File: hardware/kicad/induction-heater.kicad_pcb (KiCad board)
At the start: 2 copper layers, 21 parts, among them J1 Screw_Terminal_01x01, J2 Screw_Terminal_01x01, J3 Screw_Terminal_01x02, Q1 Q_NMOS_DGS, Q2 Q_NMOS_DGS

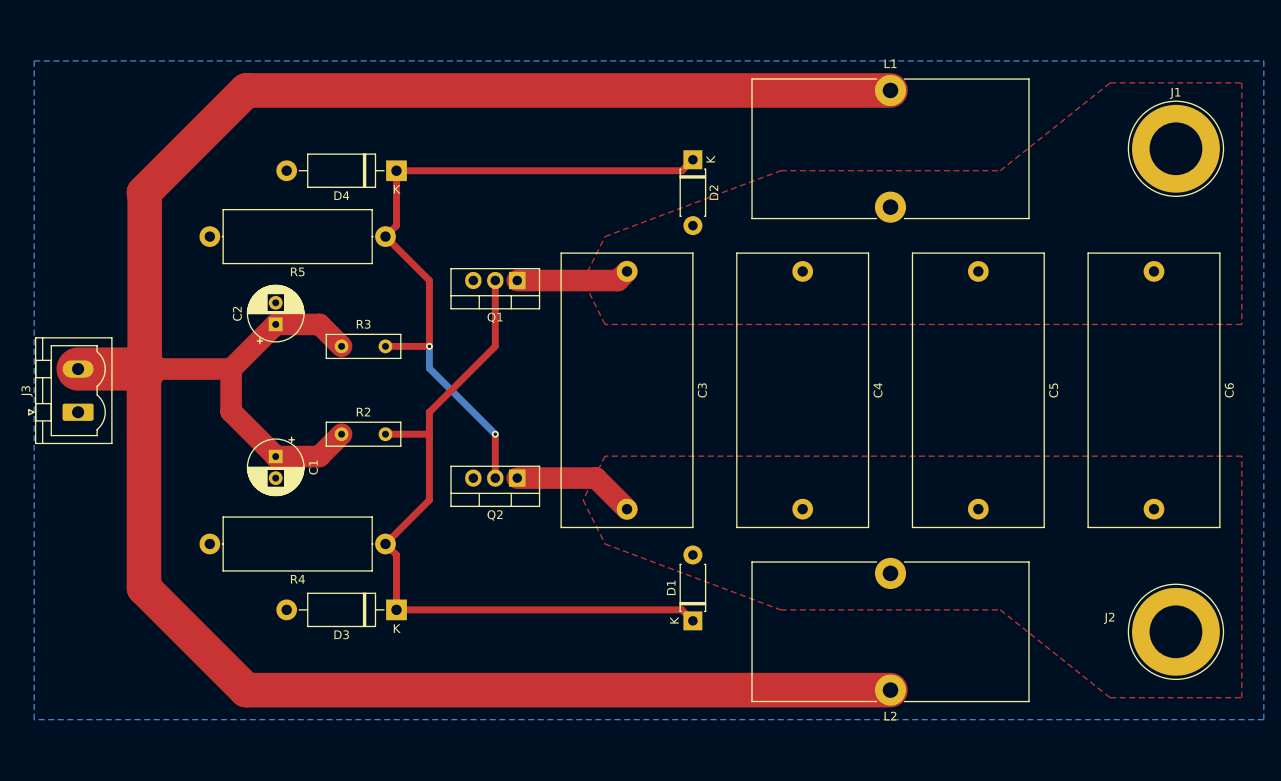
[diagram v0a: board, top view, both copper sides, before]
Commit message: Compacter board
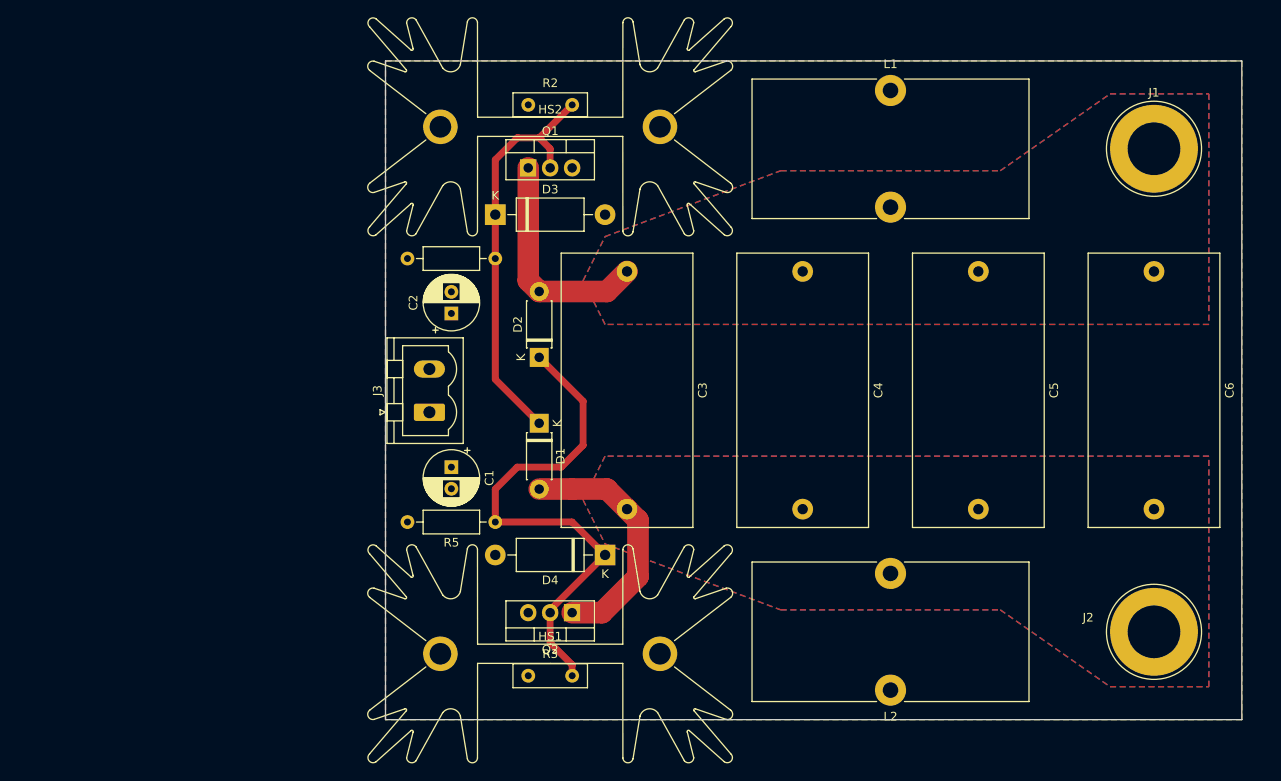
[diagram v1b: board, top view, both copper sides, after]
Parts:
- added HS1: Heatsink_Pad, Heatsink:Heatsink_Fischer_SK129-STS_42x25mm_2xDrill2.5mm, F.Cu at (146.1, 94.0)
- added HS2: Heatsink_Pad, Heatsink:Heatsink_Fischer_SK129-STS_42x25mm_2xDrill2.5mm, F.Cu at (146.1, 33.0)
- R4, R5: footprint Resistor_THT:R_Axial_DIN0617_L17.0mm_D6.0mm_P20.32mm_Horizontal -> Resistor_THT:R_Axial_DIN0207_L6.3mm_D2.5mm_P10.16mm_Horizontal
- moved D4 50.6 mm to (152.4, 82.5)
- moved D3 47.1 mm to (139.7, 43.2), turned to 0 degrees
- moved R2 43.8 mm to (143.5, 30.5)
- moved R3 43.8 mm to (143.5, 96.5)
- moved J3 40.6 mm to (132.1, 66.0)
- moved R4 35.4 mm to (139.7, 48.3)
- moved R5 35.4 mm to (139.7, 78.7)
- moved D1 29.0 mm to (144.8, 67.3), turned to -90 degrees
- moved D2 29.0 mm to (144.8, 59.7), turned to 90 degrees
- moved C2 20.4 mm to (134.6, 54.6)
- moved C1 20.4 mm to (134.6, 72.4)
- moved Q2 16.8 mm to (148.6, 89.2)
- moved Q1 13.1 mm to (143.5, 37.8), turned to 0 degrees
- moved J1 2.54 mm to (215.9, 35.6)
- moved J2 2.54 mm to (215.9, 91.4)
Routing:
- net VCC: track 282.9 -> 0.00 mm
- net Net-(D1-Pad1): track 83.8 -> 48.1 mm
- net Net-(D2-Pad1): track 81.2 -> 60.3 mm, vias 2 -> 0
- net /out_r: track 14.2 -> 28.8 mm
- net /out_l: track 16.7 -> 29.5 mm
- added copper zone on B.Cu, net /out_l
- added copper zone on B.Cu, net /out_r
- added copper zone on F.Cu, net GND
- added copper zone on B.Cu, net VCC
- removed copper zone on B.Cu, net GND
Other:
- board outline added: 99.1 x 76.2 mm

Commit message: Final touches on silkscreen
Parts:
- moved D1 1.27 mm to (143.5, 67.3)
- moved D2 1.27 mm to (143.5, 59.7)
- moved D4 1.27 mm to (152.4, 83.8)
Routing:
- net Net-(D2-Pad1): track 60.3 -> 54.6 mm
- net /out_r: track 28.8 -> 30.1 mm
- net /out_l: track 29.5 -> 30.3 mm
- net Net-(D1-Pad1): track 48.1 -> 47.6 mm
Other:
- board text added: "Gnd"
- board text added: "Vcc"
